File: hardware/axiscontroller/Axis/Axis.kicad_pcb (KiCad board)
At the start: 4 copper layers, 90 x 55 mm, 62 parts, among them J1 RS485, J10 Fan, J2 Motor, J3 Limits, J4 RS485, J5 Console, J6 Temp A, J7 Temp B, J8 Brake, J9 Power, Q1 Q_NMOS, Q2 Q_NMOS, SW1 SW_DIP_x04, U4 TLP291, U5 TLP291, U6 TLP291, U7 MAX485CPA, U8 74AHCT125

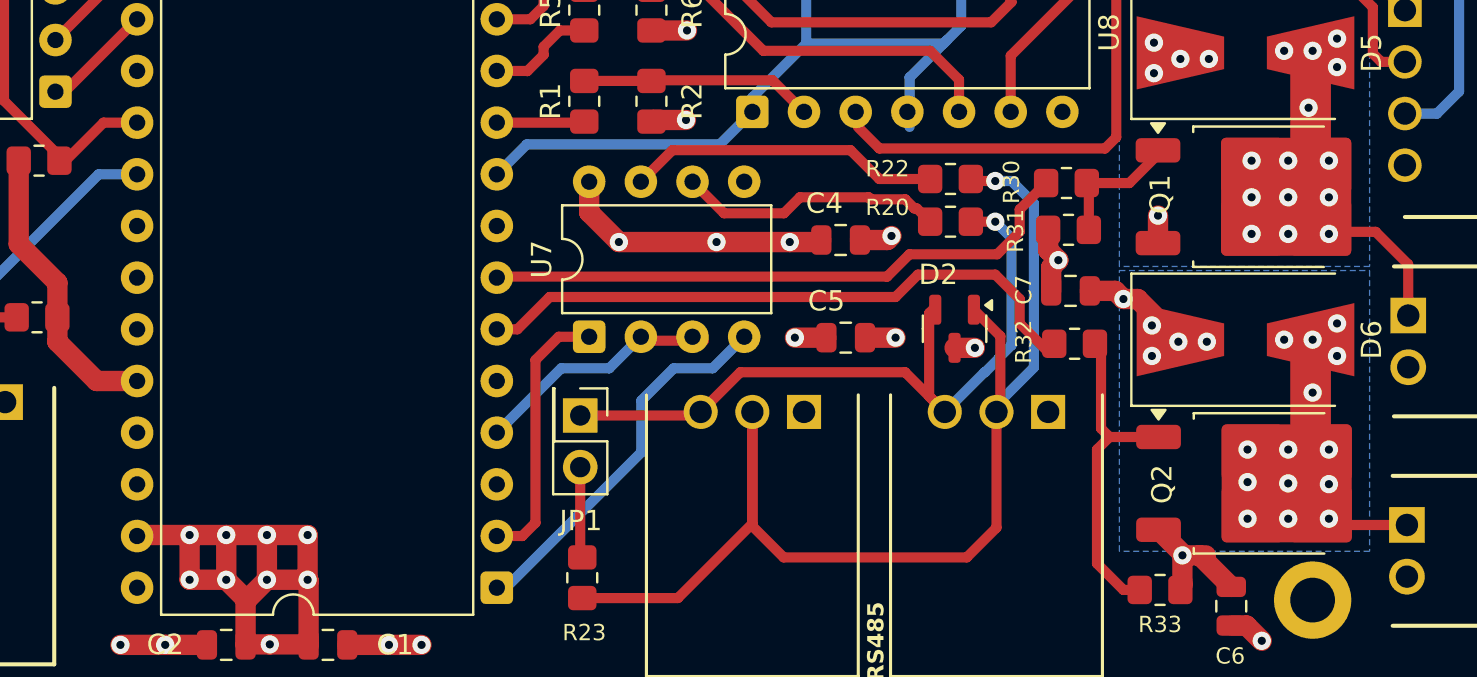
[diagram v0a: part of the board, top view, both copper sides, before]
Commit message: Fix ERC warnings/errors and add IRLR8726 component.
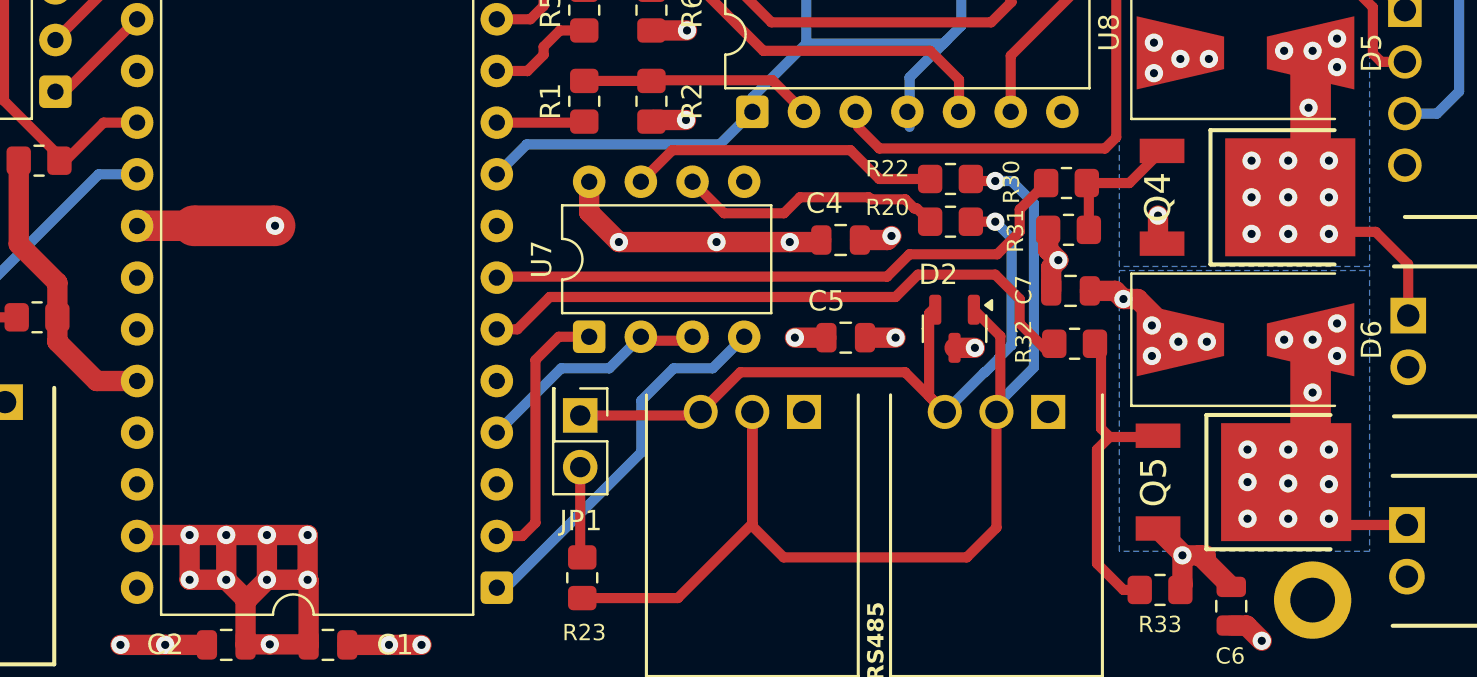
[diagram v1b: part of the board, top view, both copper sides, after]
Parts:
- removed Q1, Q2: Q_NMOS, Package_TO_SOT_SMD:TO-252-2
- added NT1: NetTie_2, NetTie:NetTie-2_SMD_Pad2.0mm, F.Cu at (201.0, 99.6)
- added Q4: IRLR8726TRPBF, AJS_Roberta:IRLR8726TRPBF, F.Cu at (250.8, 98.2)
- added Q5: IRLR8726TRPBF, AJS_Roberta:IRLR8726TRPBF, F.Cu at (250.6, 112.2)
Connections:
- A1 pad 33: GND -> Net-(A1-AGND)
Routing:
- net Net-(A1-AGND): track 0.00 -> 2.78 mm
- net GND: vias 18 -> 19

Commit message: The second revision of the robot axis controller.
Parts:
- removed A1: RaspberryPi_Pico_W, AJS_Roberta:PI_PICO2_SOCKET
- removed C1: 100nF, Capacitor_SMD:C_0805_2012Metric
- removed C2: 47uF, Capacitor_SMD:C_0805_2012Metric
- removed D6: Schottky, Diode_SMD:D_SMB-SMC_Universal_Handsoldering
- removed H2, H3: MountingHole_Pad, MountingHole:MountingHole_2.2mm_M2_DIN965_Pad
- removed J10: Fan, AJS_Roberta:MOLEX_SL_70553_0001
- removed J9: Power, AJS_Roberta:MOLEX-171857-0001
- removed JP1: Termination, Connector_PinHeader_2.54mm:PinHeader_2x01_P2.54mm_Vertical
- removed NT1: NetTie_2, NetTie:NetTie-2_SMD_Pad2.0mm
- removed U4, U5, U6: TLP291, Package_SO:SOIC-4_4.55x2.6mm_P1.27mm
- removed U8: 74AHCT125, Package_DIP:DIP-14_W7.62mm
- added C10: 10uF, Capacitor_SMD:C_0805_2012Metric, F.Cu at (210.2, 103.8)
- added C11: 47uF, Capacitor_SMD:C_0805_2012Metric, F.Cu at (198.2, 123.0)
- added C12: 22uF, Capacitor_SMD:C_0805_2012Metric, F.Cu at (193.5, 139.5)
- added C13: 47uF, Capacitor_SMD:C_0805_2012Metric, F.Cu at (256.2, 94.8)
- added C14: 4.7uF, Capacitor_SMD:C_0805_2012Metric, F.Cu at (227.0, 126.0)
- added C15: 100nF, Capacitor_SMD:C_0805_2012Metric, F.Cu at (207.5, 119.0)
- added C16: 100nF, Capacitor_SMD:C_0805_2012Metric, F.Cu at (247.5, 100.0)
- added C17: 100nF, Capacitor_SMD:C_0805_2012Metric, F.Cu at (194.2, 131.0)
- added C18: 100nF, Capacitor_SMD:C_0805_2012Metric, F.Cu at (158.7, 115.8)
- added C19: 100nF, Capacitor_SMD:C_0805_2012Metric, F.Cu at (172.0, 115.0)
- added C20: 100nF, Capacitor_SMD:C_0805_2012Metric, F.Cu at (194.5, 123.0)
- added C21: 22nF, Capacitor_SMD:C_0805_2012Metric, F.Cu at (206.0, 135.7)
- added C22: 22nF, Capacitor_SMD:C_0805_2012Metric, F.Cu at (210.5, 141.2)
- added C23: 22nF, Capacitor_SMD:C_0805_2012Metric, F.Cu at (197.8, 131.8)
- added C24: 22uF, Capacitor_SMD:C_0805_2012Metric, F.Cu at (167.7, 130.8)
- added C25: 1uF, Capacitor_SMD:C_0805_2012Metric, F.Cu at (166.9, 137.0)
- added C9: 100nF, Capacitor_SMD:C_0805_2012Metric, F.Cu at (213.2, 123.8)
- added D10: Schottky, Diode_SMD:D_SMB-SMC_Universal_Handsoldering, F.Cu at (177.5, 96.0)
- added D11: Schottky, Diode_SMD:D_SMB-SMC_Universal_Handsoldering, F.Cu at (170.0, 96.0)
- added D4: CLMUD_FKC, AJS_Cree:CLMVC-FKC-CG1J1561BB7D3S3, F.Cu at (249.1, 82.2)
- added D7: Schottky, Diode_SMD:D_SMB-SMC_Universal_Handsoldering, F.Cu at (185.0, 96.0)
- added FB1: FerriteBead_Small, Inductor_SMD:L_0805_2012Metric, F.Cu at (164.5, 117.0)
- added FB2: FerriteBead_Small, Inductor_SMD:L_0805_2012Metric, F.Cu at (164.5, 127.0)
- added IC1: ESP32-S3-WROOM-1U-N16R8, AJS_Espressif:ESP32-S-3WROOM-1U-N16R8, F.Cu at (181.3, 130.8)
- added IC2: TCA6507PWR, AJS_TexasInstruments:TCA6507PWR, F.Cu at (252.2, 97.0)
- added IC3: STM32G071KBT3TR, AJS_STMicro:STM32G071KBT3TR, F.Cu at (220.5, 120.8)
- added IC4: AT21CS01-STUM10-T, AJS_STMicro:AT21CS01-STUM10-T, F.Cu at (226.0, 134.4)
- added J12: TC2050, Connector:Tag-Connect_TC2050-IDC-FP_2x05_P1.27mm_Vertical, F.Cu at (195.2, 112.6)
- added J17: JST PH, Connector_JST:JST_PH_S2B-PH-K_1x02_P2.00mm_Horizontal, F.Cu at (179.2, 86.5)
- added J18: JST PH, Connector_JST:JST_PH_S8B-PH-K_1x08_P2.00mm_Horizontal, F.Cu at (205.8, 86.5)
- added J19: JST PH, Connector_JST:JST_PH_S2B-PH-K_1x02_P2.00mm_Horizontal, F.Cu at (186.2, 86.5)
- added J20: JST PH, Connector_JST:JST_PH_S2B-PH-K_1x02_P2.00mm_Horizontal, F.Cu at (172.2, 86.5)
- added J21: JST PH, Connector_JST:JST_PH_S2B-PH-K_1x02_P2.00mm_Horizontal, F.Cu at (257.5, 86.5)
- added J22: JST PH, Connector_JST:JST_PH_S2B-PH-K_1x02_P2.00mm_Horizontal, F.Cu at (264.8, 86.5)
- added Q6: IRLR8726TRPBF, AJS_Roberta:IRLR8726TRPBF, F.Cu at (184.2, 107.8)
- added Q7: IRLR8726TRPBF, AJS_Roberta:IRLR8726TRPBF, F.Cu at (176.5, 107.8)
- added Q8: IRLR8726TRPBF, AJS_Roberta:IRLR8726TRPBF, F.Cu at (168.8, 107.8)
- added Q9: 2N7002, Package_TO_SOT_SMD:SOT-23, F.Cu at (228.6, 94.0)
- added R24: 4700, Resistor_SMD:R_0805_2012Metric, F.Cu at (204.8, 103.8)
- added R25: 33, Resistor_SMD:R_0805_2012Metric, F.Cu at (194.2, 134.0)
- added R26: 100K, Resistor_SMD:R_0805_2012Metric, F.Cu at (223.2, 102.2)
- added R27: 100, Resistor_SMD:R_0805_2012Metric, F.Cu at (255.1, 126.0)
- added R28: 4K7, Resistor_SMD:R_0805_2012Metric, F.Cu at (208.5, 137.3)
- added R34: 100, Resistor_SMD:R_0805_2012Metric, F.Cu at (186.1, 115.0)
- added R35: 10000, Resistor_SMD:R_0805_2012Metric, F.Cu at (256.5, 91.5)
- added R36: 10000, Resistor_SMD:R_0805_2012Metric, F.Cu at (182.5, 115.0)
- added R37: 100, Resistor_SMD:R_0805_2012Metric, F.Cu at (179.0, 115.0)
- added R38: 10000, Resistor_SMD:R_0805_2012Metric, F.Cu at (175.5, 115.0)
- added R39: 100K, Resistor_SMD:R_0805_2012Metric, F.Cu at (204.5, 119.0)
- added R40: 100, Resistor_SMD:R_0805_2012Metric, F.Cu at (164.0, 111.8)
- added R41: 100, Resistor_SMD:R_0805_2012Metric, F.Cu at (207.5, 115.5)
- added R42: 1K0, Resistor_SMD:R_0805_2012Metric, F.Cu at (222.8, 134.9)
- added R44: 10000, Resistor_SMD:R_0805_2012Metric, F.Cu at (161.8, 109.2)
- added R45: 1000, Resistor_SMD:R_0805_2012Metric, F.Cu at (196.8, 91.2)
- added R46: 4700, Resistor_SMD:R_0805_2012Metric, F.Cu at (194.8, 103.8)
- added R47: 100, Resistor_SMD:R_0805_2012Metric, F.Cu at (197.2, 103.8)
- added R48: 1000, Resistor_SMD:R_0805_2012Metric, F.Cu at (191.5, 91.2)
- added R49: 4700, Resistor_SMD:R_0805_2012Metric, F.Cu at (189.8, 103.8)
- added R50: 100, Resistor_SMD:R_0805_2012Metric, F.Cu at (192.2, 103.8)
- added R51: 100K, Resistor_SMD:R_0805_2012Metric, F.Cu at (227.2, 102.2)
- added R52: 100, Resistor_SMD:R_0805_2012Metric, F.Cu at (227.2, 105.2)
- added R53: 100, Resistor_SMD:R_0805_2012Metric, F.Cu at (223.2, 105.2)
- added R54: 330, Resistor_SMD:R_0805_2012Metric, F.Cu at (249.8, 85.8)
- added R55: 100, Resistor_SMD:R_0805_2012Metric, F.Cu at (253.6, 115.0)
- added R56: R_10K, Resistor_SMD:R_0805_2012Metric, F.Cu at (168.2, 133.8)
- added R57: 4K7, Resistor_SMD:R_0805_2012Metric, F.Cu at (210.5, 144.8)
- added R58: 4K7, Resistor_SMD:R_0805_2012Metric, F.Cu at (201.2, 131.8)
- added R59: R_10K, Resistor_SMD:R_0805_2012Metric, F.Cu at (196.8, 137.5)
- added R60: 330, Resistor_SMD:R_0805_2012Metric, F.Cu at (249.8, 88.0)
- added R61: 330, Resistor_SMD:R_0805_2012Metric, F.Cu at (249.8, 90.2)
- added R62: 330, Resistor_SMD:R_0805_2012Metric, F.Cu at (223.5, 86.0)
- added R63: 330, Resistor_SMD:R_0805_2012Metric, F.Cu at (223.5, 88.2)
- added R64: 330, Resistor_SMD:R_0805_2012Metric, F.Cu at (223.5, 90.5)
- added R65: 33, Resistor_SMD:R_0805_2012Metric, F.Cu at (236.5, 119.5)
- added R66: 33, Resistor_SMD:R_0805_2012Metric, F.Cu at (232.5, 117.9)
- added R67: 33, Resistor_SMD:R_0805_2012Metric, F.Cu at (204.1, 113.0)
- added R68: 33, Resistor_SMD:R_0805_2012Metric, F.Cu at (204.5, 116.8)
- added R69: 33, Resistor_SMD:R_0805_2012Metric, F.Cu at (254.0, 103.2)
- added R70: 4K7, Resistor_SMD:R_0805_2012Metric, F.Cu at (251.2, 103.8)
- added R71: 4K7, Resistor_SMD:R_0805_2012Metric, F.Cu at (248.2, 104.0)
- added SW2: SW_Tactile_6mm, AJS_SameSky:Tactile_6mm_6mm_4.5mm, F.Cu at (163.4, 143.8)
- added SW3: SW_Tactile_6mm, AJS_SameSky:Tactile_6mm_6mm_4.5mm, F.Cu at (201.6, 143.8)
- added U11: TLP291, Package_SO:SOIC-4_4.55x2.6mm_P1.27mm, F.Cu at (201.8, 97.0)
- added U12: TLP291, Package_SO:SOIC-4_4.55x2.6mm_P1.27mm, F.Cu at (196.8, 97.0)
- added U13: TLP291, Package_SO:SOIC-4_4.55x2.6mm_P1.27mm, F.Cu at (191.5, 97.0)
- added U14: MAX485CPA, Package_SO:SOIC-8_3.9x4.9mm_P1.27mm, F.Cu at (196.2, 127.0)
- added U2: AMS1117-3.3, Package_TO_SOT_SMD:SOT-223-3_TabPin2, F.Cu at (216.5, 102.8)
- added U9: TLP291, Package_SO:SOIC-4_4.55x2.6mm_P1.27mm, F.Cu at (207.0, 97.0)
- added Y4: 8MHz, Crystal:Resonator_SMD_Murata_CSTxExxV-3Pin_3.0x1.1mm, F.Cu at (218.9, 127.7)
- C3: value 100nF -> 10uF
- D2: value SM712_SOT23 -> USBLC6-2SC6Y; footprint Package_TO_SOT_SMD:SOT-23 -> AJS_STMicro:USBLC6-2SC6Y
- D5: value Schottky -> CLMUD_FKC; footprint Diode_SMD:D_SMB-SMC_Universal_Handsoldering -> AJS_Cree:CLMVC-FKC-CG1J1561BB7D3S3
- H1: value MountingHole_Pad -> MountingHole; footprint MountingHole:MountingHole_2.2mm_M2_DIN965_Pad -> MountingHole:MountingHole_6.5mm
- J1: value RS485 -> Conn_01x04_Pin; footprint AJS_Roberta:MOLEX_SL_70553_0002 -> Connector_PinHeader_2.54mm:PinHeader_1x04_P2.54mm_Vertical
- J2: value Motor -> CL57_Driver; footprint AJS_Roberta:MOLEX_SL_70553_0003 -> Connector_JST:JST_PH_S9B-PH-K_1x09_P2.00mm_Horizontal
- J3: value Limits -> ~; footprint AJS_Roberta:MOLEX_SL_70553_0003 -> AJS_Molex:KK254-171857-0004
- J4: value RS485 -> Conn_02x12_Counter_Clockwise; footprint AJS_Roberta:MOLEX_SL_70553_0002 -> AJS_UProbe:MicroRing24x20
- J5: value Console -> USBC-217179-0001; footprint AJS_Roberta:MOLEX_SL_70553_0002 -> AJS_Molex:USBC-217179-0001
- J6: value Temp A -> TE MicroMatch; footprint AJS_Roberta:MOLEX_SL_70553_0001 -> AJS_TEConnectivity:MicroMatch_Locking_3380708
- J7: value Temp B -> ~; footprint AJS_Roberta:MOLEX_SL_70553_0001 -> Connector_PinHeader_2.54mm:PinHeader_1x08_P2.54mm_Vertical
- J8: value Brake -> Conn_01x04_Pin; footprint AJS_Roberta:MOLEX_SL_70553_0001 -> Connector_PinHeader_2.54mm:PinHeader_1x04_P2.54mm_Vertical
- Q4, Q5: value IRLR8726TRPBF -> 2N7002; footprint AJS_Roberta:IRLR8726TRPBF -> Package_TO_SOT_SMD:SOT-23
- R1: value 100 -> 5K1; footprint Resistor_SMD:R_0805_2012Metric_Pad1.20x1.40mm_HandSolder -> Resistor_SMD:R_0805_2012Metric
- R10: value 10000 -> 33; footprint Resistor_SMD:R_0805_2012Metric_Pad1.20x1.40mm_HandSolder -> Resistor_SMD:R_0805_2012Metric
- R11: value 1000 -> 0; footprint Resistor_SMD:R_0805_2012Metric_Pad1.20x1.40mm_HandSolder -> Resistor_SMD:R_0805_2012Metric
- R12: value 470 -> 33; footprint Resistor_SMD:R_0805_2012Metric_Pad1.20x1.40mm_HandSolder -> Resistor_SMD:R_0805_2012Metric
- R13, R33: value 10000 -> 100; footprint Resistor_SMD:R_0805_2012Metric_Pad1.20x1.40mm_HandSolder -> Resistor_SMD:R_0805_2012Metric
- R14, R17: value 1000 -> 100k; footprint Resistor_SMD:R_0805_2012Metric_Pad1.20x1.40mm_HandSolder -> Resistor_SMD:R_0805_2012Metric
- R15, R18: value 4700 -> 0; footprint Resistor_SMD:R_0805_2012Metric_Pad1.20x1.40mm_HandSolder -> Resistor_SMD:R_0805_2012Metric
- R16, R19, R20, R22, R23, R29, R3, R30: footprint Resistor_SMD:R_0805_2012Metric_Pad1.20x1.40mm_HandSolder -> Resistor_SMD:R_0805_2012Metric
- R2: value 10000 -> 5K1; footprint Resistor_SMD:R_0805_2012Metric_Pad1.20x1.40mm_HandSolder -> Resistor_SMD:R_0805_2012Metric
- R21, R31: value 10000 -> 1000; footprint Resistor_SMD:R_0805_2012Metric_Pad1.20x1.40mm_HandSolder -> Resistor_SMD:R_0805_2012Metric
- R32: value 100 -> 4700; footprint Resistor_SMD:R_0805_2012Metric_Pad1.20x1.40mm_HandSolder -> Resistor_SMD:R_0805_2012Metric
- R4: value 470 -> 4K7; footprint Resistor_SMD:R_0805_2012Metric_Pad1.20x1.40mm_HandSolder -> Resistor_SMD:R_0805_2012Metric
- R5: value 100 -> 100K; footprint Resistor_SMD:R_0805_2012Metric_Pad1.20x1.40mm_HandSolder -> Resistor_SMD:R_0805_2012Metric
- R6: value 10000 -> 47; footprint Resistor_SMD:R_0805_2012Metric_Pad1.20x1.40mm_HandSolder -> Resistor_SMD:R_0805_2012Metric
- R7: value 4700 -> 100k; footprint Resistor_SMD:R_0805_2012Metric_Pad1.20x1.40mm_HandSolder -> Resistor_SMD:R_0805_2012Metric
- R8: value 470 -> 47; footprint Resistor_SMD:R_0805_2012Metric_Pad1.20x1.40mm_HandSolder -> Resistor_SMD:R_0805_2012Metric
- R9: value 100 -> 120; footprint Resistor_SMD:R_0805_2012Metric_Pad1.20x1.40mm_HandSolder -> Resistor_SMD:R_0805_2012Metric
- SW1: value SW_DIP_x04 -> SW_Tactile_6mm; footprint Package_DIP:DIP-8_W7.62mm -> AJS_SameSky:Tactile_6mm_6mm_4.5mm
- U7: footprint Package_DIP:DIP-8_W7.62mm -> Package_SO:SOIC-8_3.9x4.9mm_P1.27mm
- moved J8 104.9 mm to (173.0, 144.5), turned to 90 degrees
- moved H1 94.2 mm to (161.0, 86.2)
- moved J7 92.5 mm to (262.5, 125.7), turned to 180 degrees
- moved R4 89.7 mm to (161.5, 115.0), turned to 90 degrees
- moved J5 83.9 mm to (158.8, 122.2), turned to -90 degrees
- moved J6 82.4 mm to (269.5, 121.4), turned to 90 degrees
- moved C7 78.3 mm to (164.0, 108.0), turned to -90 degrees
- moved D2 73.2 mm to (165.2, 122.0), turned to 0 degrees
- moved R29 72.5 mm to (263.8, 91.5), turned to 0 degrees
- moved R12 67.0 mm to (201.8, 136.2)
- moved R2 64.9 mm to (164.8, 125.0), turned to 0 degrees
- moved R5 64.4 mm to (158.8, 113.8), turned to 180 degrees
- moved R8 63.6 mm to (202.2, 126.5), turned to 180 degrees
- moved C6 61.8 mm to (189.0, 108.5), turned to -90 degrees
- moved R1 59.2 mm to (164.8, 119.0), turned to 0 degrees
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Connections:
- C4 pad 1: +5V -> +3V3
- C5 pad 1: +5V -> +3V3
- D2 pad 1: Net-(D2-A1) -> Net-(D2-I/O1_1)
- D2 pad 2: Net-(D2-A2) -> GND
- D2 pad 3: GND -> Net-(D2-I/O2_1)
- D5 pad 1: +12V -> +3V3
- D5 pad 2: Net-(D5-A) -> Net-(D5-RK)
- J1 pad 1: GND -> +3V3
- J1 pad 2: Net-(D2-A1) -> /Master/CONSOLE_RX
- J1 pad 3: Net-(D2-A2) -> /Master/CONSOLE_TX
- J2 pad 1: /ENA -> /PUL+
- J2 pad 2: /DIR -> /PUL-
- J2 pad 3: /PUL -> /DIR+
- J2 pad 4: GND -> /DIR-
- J3 pad 1: GND -> +5V
- J3 pad 2: /HOME -> GND
- J3 pad 3: /LIMIT_A -> GND
- J3 pad 4: /LIMIT_B -> +12V
- J4 pad 1: GND -> /LIMIT_A
- J4 pad 2: Net-(D2-A1) -> /LIMIT_B
- J4 pad 3: Net-(D2-A2) -> /LIMIT_C
- J6 pad 2: Net-(A1-GPIO27_ADC1) -> /BOOT
- J7 pad 2: Net-(A1-GPIO26_ADC0) -> /BOOT
- J8 pad 1: Net-(D5-A) -> /Master/TCK
- J8 pad 2: +12V -> /Master/TDO
- Q4 pad 2: Net-(D5-A) -> GND
- Q4 pad 3: GND -> /PUL-
- Q5 pad 2: Net-(D6-A) -> GND
- Q5 pad 3: GND -> /DIR-
- R1 pad 1: /MCU_PUL -> Net-(J5-CC1)
- R1 pad 2: Net-(R1-Pad2) -> GND
- R10 pad 1: GND -> /Master/MCU_BOOT
- R10 pad 2: Net-(R10-Pad2) -> /BOOT
- R11 pad 1: +12V -> +5V
- R11 pad 2: Net-(R11-Pad2) -> /PUL+
- R12 pad 1: Net-(R12-Pad1) -> /Master/MCU_ESTOP
- R12 pad 2: /ENA -> /ESTOP
- R13 pad 1: /MOTOR_OE -> /MCU_DIR
- R13 pad 2: +5V -> Net-(Q5-G)
- R14 pad 1: +12V -> GND
- R14 pad 2: Net-(R14-Pad2) -> Net-(Q5-G)
- R15 pad 1: Net-(R15-Pad1) -> +5V
- R15 pad 2: +5V -> /DIR+
- R16 pad 1: Net-(R15-Pad1) -> /MCU_ENA
- R16 pad 2: /MCU_LIMIT_B -> Net-(Q9-G)
- R17 pad 1: +12V -> GND
- R17 pad 2: Net-(R17-Pad2) -> Net-(Q9-G)
- R18 pad 1: Net-(R18-Pad1) -> +5V
- R18 pad 2: +5V -> /ENA+
- R19 pad 1: Net-(R18-Pad1) -> /ESTOP
- R19 pad 2: /MCU_HOME -> /MicroController/ESTOP
- R2 pad 1: GND -> Net-(J5-CC2)
- R2 pad 2: Net-(R1-Pad2) -> GND
- R20 pad 1: Net-(D2-A2) -> /RS485_A
- R21 pad 1: Net-(A1-GPIO27_ADC1) -> +12V
- R21 pad 2: +3V3 -> Net-(R21-Pad2)
- R22 pad 1: Net-(D2-A1) -> /RS485_B
- R23 pad 1: Net-(JP1-B) -> /RS485_A
- R23 pad 2: Net-(D2-A1) -> /RS485_B
- R29 pad 1: Net-(A1-GPIO26_ADC0) -> /MicroController/TEMP_B
- R3 pad 1: Net-(R3-Pad1) -> /MCU_PUL
- R3 pad 2: /MCU_LIMIT_A -> Net-(Q4-G)
- R30 pad 1: Net-(Q4-G) -> Net-(R24-Pad1)
- R30 pad 2: /MCU_BRAKE -> /LIMIT_A
- R31 pad 1: Net-(Q4-G) -> +12V
- R31 pad 2: GND -> Net-(R31-Pad2)
- R32 pad 1: Net-(Q5-G) -> Net-(R32-Pad1)
- R32 pad 2: /MCU_FAN -> +3V3
- R33 pad 1: Net-(Q5-G) -> Net-(R32-Pad1)
- R33 pad 2: GND -> /LIMIT_B
- R4 pad 1: Net-(R4-Pad1) -> Net-(D2-VBUS)
- R4 pad 2: /PUL -> /Master/USB_SENSE
- R5 pad 1: /MCU_DIR -> /Master/USB_SENSE
- R5 pad 2: Net-(R5-Pad2) -> GND
- R6 pad 1: GND -> /RS485_A
- R6 pad 2: Net-(R5-Pad2) -> Net-(U14-A)
- R7 pad 1: Net-(R3-Pad1) -> GND
- R7 pad 2: +5V -> Net-(Q4-G)
- R8 pad 1: Net-(R8-Pad1) -> /RS485_B
- R8 pad 2: /DIR -> Net-(U14-B)
- R9 pad 1: /MCU_ENA -> /RS485_A
- R9 pad 2: Net-(R10-Pad2) -> /RS485_B
- SW1 pad 1: /ADDR0 -> GND
- SW1 pad 2: /ADDR1 -> /MicroController/NRST
- U7 pad 1: /RS485_RX -> /MicroController/RS485_RX
- U7 pad 2: /RS485_DIR -> /MicroController/RS485_DIR
- U7 pad 3: /RS485_DIR -> /MicroController/RS485_DIR
- U7 pad 4: /RS485_TX -> /MicroController/RS485_TX
- U7 pad 8: +5V -> +3V3
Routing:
- net /ESTOP: track 0.00 -> 109.3 mm, vias 0 -> 1
- net /SYNC: track 0.00 -> 107.8 mm, vias 0 -> 1
- net /BOOT: track 0.00 -> 99.7 mm, vias 0 -> 1
- net GND: track 37.1 -> 135.6 mm, vias 19 -> 63
- net /RS485_A: track 0.00 -> 97.2 mm, vias 0 -> 1
- net /RS485_B: track 0.00 -> 96.6 mm, vias 0 -> 1
- net +3V3: track 14.4 -> 80.1 mm, vias 0 -> 28
- net /OP_SPARE: track 0.00 -> 64.0 mm
- net Net-(D2-A1): track 60.2 -> 0.00 mm, vias 1 -> 0
- net /MicroController/BOOT: track 0.00 -> 60.0 mm
- net Net-(IC1-EN): track 0.00 -> 49.8 mm, vias 0 -> 2
- net /MicroController/NRST: track 0.00 -> 48.0 mm, vias 0 -> 3
- net +5V: track 57.9 -> 10.1 mm, vias 16 -> 4
- net /MicroController/TEMP_B: track 0.00 -> 46.1 mm, vias 0 -> 2
- net /MicroController/TEMP_A: track 0.00 -> 44.8 mm, vias 0 -> 2
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- added copper zone on In2.Cu, net +12V
- added copper zone on In2.Cu, net +3V3
- added copper zone on In2.Cu, net +5V
- added copper zone on In1.Cu, net GND
- removed copper zone on In1.Cu, net +12V
- removed copper zone on In1.Cu, net +5V
- removed copper zone on In2.Cu, net GND
- removed copper zone on B.Cu, net Net-(D5-A)
- removed copper zone on B.Cu, net Net-(D6-A)
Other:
- board size 90 x 55 mm -> 116 x 69 mm
- board text added: "8MHz"
- board text added: "ALM"
- board text added: "Antenna cable strain relied Antenna mounting hole Thermal pad cutout under ESP32 3D model on opto couplers"
- board text added: "BOOT"
- board text added: "BRK"
- board text added: "COM"
- board text added: "DIR+"
- board text added: "DIR-"
- board text added: "ENA+"
- board text added: "ENA-"
- board text added: "ESTOP"
- board text added: "L1"
- board text added: "L2"
- board text added: "L3"
- board text added: "L4"
- board text added: "MASTER BOOT"
- board text added: "MASTER RESET"
- board text added: "OPA"
- board text added: "OPB"
- board text added: "OPC"
- board text added: "PUL+"
- board text added: "PUL-"
- board text added: "RS485A"
- board text added: "RS485B"
- board text added: "SLAVE RESET"
- board text added: "SYNC+"
- board text added: "SYNC-"
- board text added: "TEMPA"
- board text added: "TEMPB"
- board text removed: "18mm"
- board text removed: "22mm"
- board text removed: "33mm"
- board text removed: "4mm"
- board text removed: "72mm"
- board text removed: "A"
- board text removed: "B"
- board text removed: "BRAKE"
- board text removed: "BRAKE+"
- board text removed: "BRAKE-"
- board text removed: "CONSOLE"
- board text removed: "DIR"
- board text removed: "ENA"
- board text removed: "FAN"
- board text removed: "FAN+"
- board text removed: "FAN-"
- board text removed: "HOME"
- board text removed: "LIMIT A"
- board text removed: "LIMIT B"
- board text removed: "LIMITS"
- board text removed: "M2"
- board text removed: "MOTOR"
- board text removed: "POWER"
- board text removed: "PUL"
- board text removed: "RS485"
- board text removed: "RX"
- board text removed: "Rev A, AJS Contract Design Ltd, 2025"
- board text removed: "SENSOR"
- board text removed: "Single Axis Controller"
- board text removed: "TEMP A"
- board text removed: "TEMP B"
- board text removed: "TX"
